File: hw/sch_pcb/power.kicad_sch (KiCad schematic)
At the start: 17 parts, among them U2 LMR16006YDDCT, U3 MCP1700, U4 MCP1700

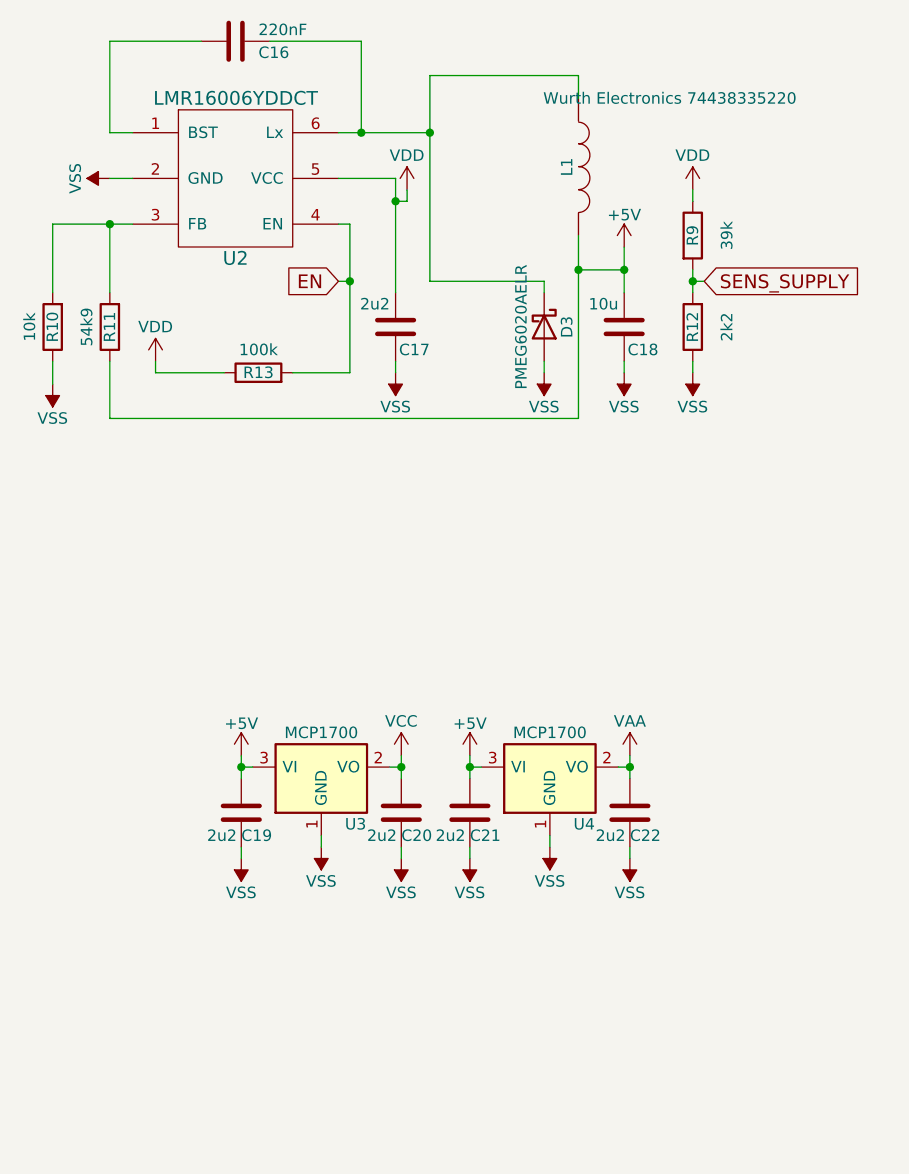
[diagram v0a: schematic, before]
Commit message: CAN interface connector added #3
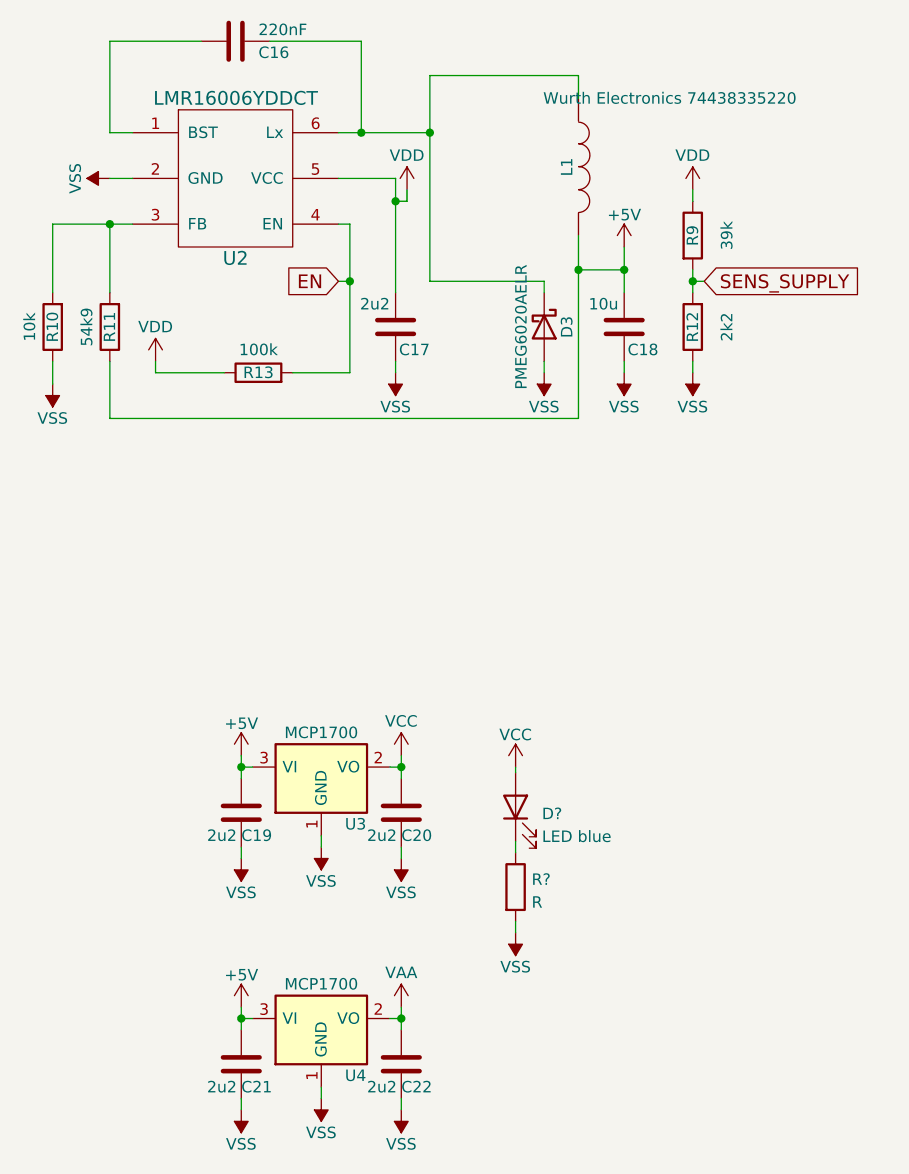
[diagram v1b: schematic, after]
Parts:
- added D?: LED blue, symbol Device:LED
- added R?: R, symbol Device:R
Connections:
- net VCC: now also D?.2 (A)
- net VSS: now also R?.2
- new net: D?.1 (K), R?.1
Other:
- moved on the sheet: C21, C22, U4
